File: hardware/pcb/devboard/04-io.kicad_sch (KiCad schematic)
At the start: 14 parts, among them J10 EXTENSION (non monte), J13 CLAVIER INTERNE, J6 USB-C CHARGE + PROG, J7 USB-C CLAVIER (hote), J8 microSD

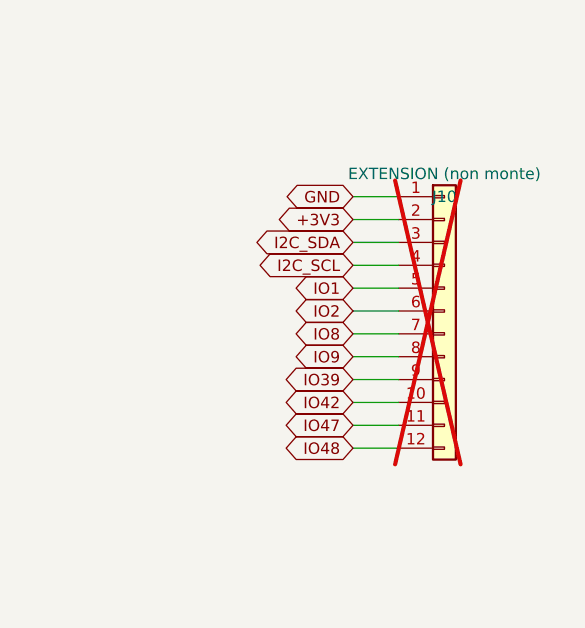
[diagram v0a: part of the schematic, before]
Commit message: feat(pcb): ready the dev board for fabrication
- drop J10, the unpopulated extension header (schematic + copper)
- extend the In2.Cu +3V3 plane to the left board edge, closing the
  gap under the DevKitC headers, and refill the zones
- mark J11/J12 (DevKitC header rows) DNP for hand-soldering; give J13
  (internal-keyboard JST-PH S4B-PH-K) its LCSC C157926 for fab assembly
- add the dev board BOM source
- gen_fab: apply J13's +180 JLCPCB rotation, matching the other JST-PH
- check_pcb: treat an absent USB pair as not-present, not "unrouted"
  (USB_PROG only exists on the mainboard)

Co-Authored-By: Claude Opus 4.8 <noreply@anthropic.com>
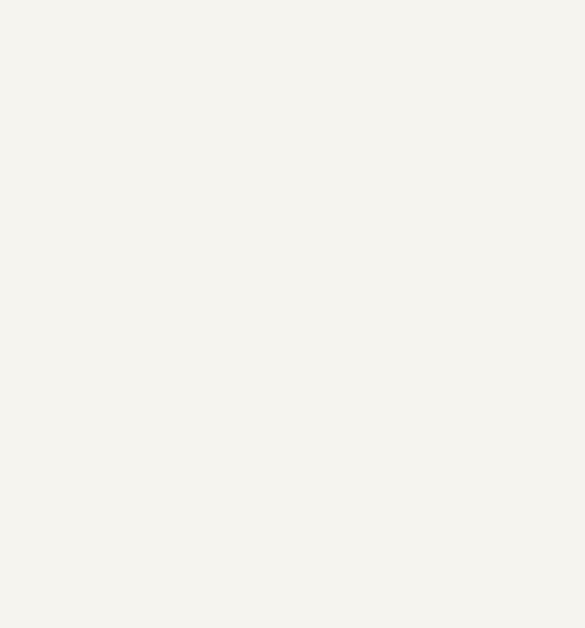
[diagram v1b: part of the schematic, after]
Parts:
- removed J10: EXTENSION (non monte), Connector_PinHeader_2.54mm:PinHeader_1x12_P2.54mm_Vertical, symbol Connector_Generic:Conn_01x12
- J13: LCSC (none) -> C157926; MPN (none) -> S4B-PH-K-S

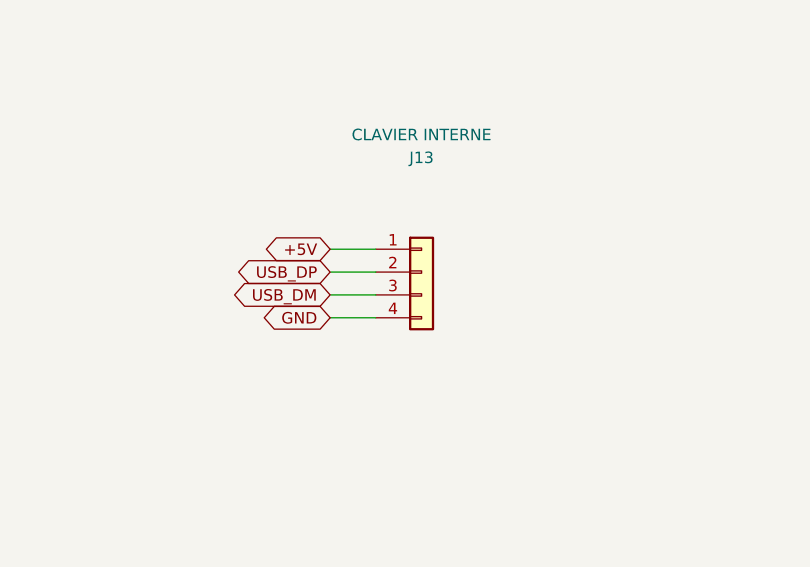
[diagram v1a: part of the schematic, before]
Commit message: feat(pcb): cost-optimize the dev board for JLCPCB
- shrink the outline to 99 x 45 mm and recenter MH2/MH4, keeping every
  dimension under 100 mm to dodge the large-board engineering fee
- reshape the In2.Cu +5V plane, restore the GND_surface pour, refill zones
- widen the main VBUS run to 1.2 mm, clearing the G2 thermal warning
- mark J1/J2/J3/J13 (JST-PH) and SW1 DNP: hand-soldered, so the board is
  all-SMD and skips the through-hole wave-solder fixture
- move R1/R10/R11/R26/R27 to Basic 0603 (150R/56k/7.5k), dropping three
  extended feeders; values and the 5V feedback ratio preserved
- swap D1 to the promotional SMF5.0A C19077497 (identical part, fee waived)
- gen_fab: J13 takes no JLCPCB rotation correction (verified in preview)

Co-Authored-By: Claude Opus 4.8 <noreply@anthropic.com>
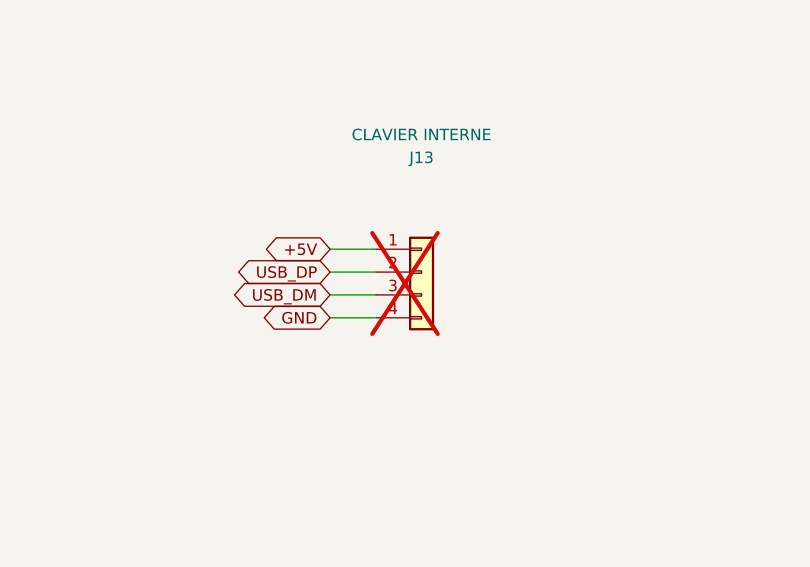
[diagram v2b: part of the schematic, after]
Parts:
- J13: now not fitted
- R26, R27: footprint Resistor_SMD:R_0402_1005Metric -> Resistor_SMD:R_0603_1608Metric; LCSC C25796 -> C23206; MPN 0402WGF5602TCE -> 0603WAF5602T5E
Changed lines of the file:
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@@
 			)
 		)
-		(property "Footprint" "Resistor_SMD:R_0402_1005Metric"
+		(property "Footprint" "Resistor_SMD:R_0603_1608Metric"
 			(at 414.02 43.18000000000001 0)
 			(effects
@@
 			(hide yes)
 		)
-		(property "LCSC" "C25796"
+		(property "LCSC" "C23206"
 			(at 414.02 35.56 0)
 			(effects
@@
 			(hide yes)
 		)
-		(property "MPN" "0402WGF5602TCE"
+		(property "MPN" "0603WAF5602T5E"
 			(at 414.02 33.02000000000001 0)
 			(effects
@@
 			)
 		)
-		(property "Footprint" "Resistor_SMD:R_0402_1005Metric"
+		(property "Footprint" "Resistor_SMD:R_0603_1608Metric"
 			(at 490.22 43.18000000000001 0)
 			(effects
@@
 			(hide yes)
 		)
-		(property "LCSC" "C25796"
+		(property "LCSC" "C23206"
 			(at 490.22 35.56 0)
 			(effects
@@
 			(hide yes)
 		)
-		(property "MPN" "0402WGF5602TCE"
+		(property "MPN" "0603WAF5602T5E"
 			(at 490.22 33.02000000000001 0)
 			(effects
@@
 		(in_bom yes)
 		(on_board yes)
-		(dnp no)
+		(dnp yes)
 		(fields_autoplaced yes)
 		(property "Reference" "J13"
